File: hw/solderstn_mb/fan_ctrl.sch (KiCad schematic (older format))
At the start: 9 parts, among them M601 Fan_4pin, Q601 DMG1012T, U601 74LVC2G17gw

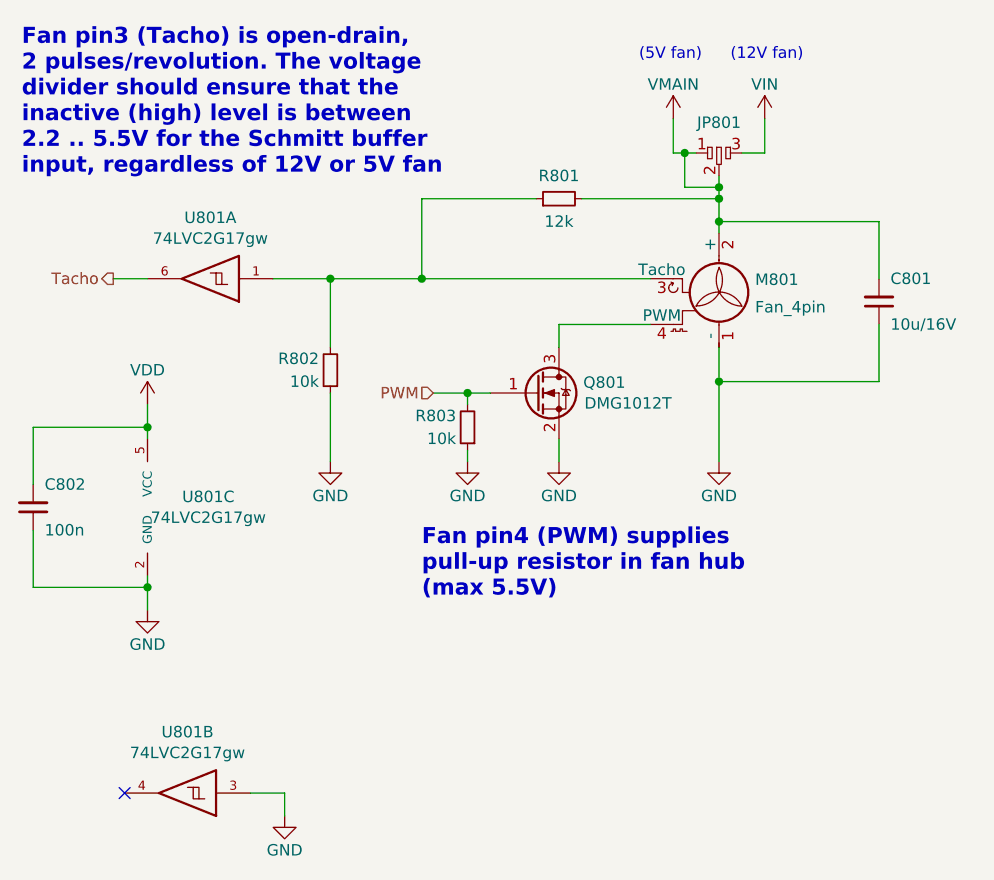
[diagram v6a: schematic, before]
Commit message: MB: 1) remove 2x fan ctrls 2) MCU pin-out for a VS1063 3) add VS1063 DSP/codec to audio path (WIP)
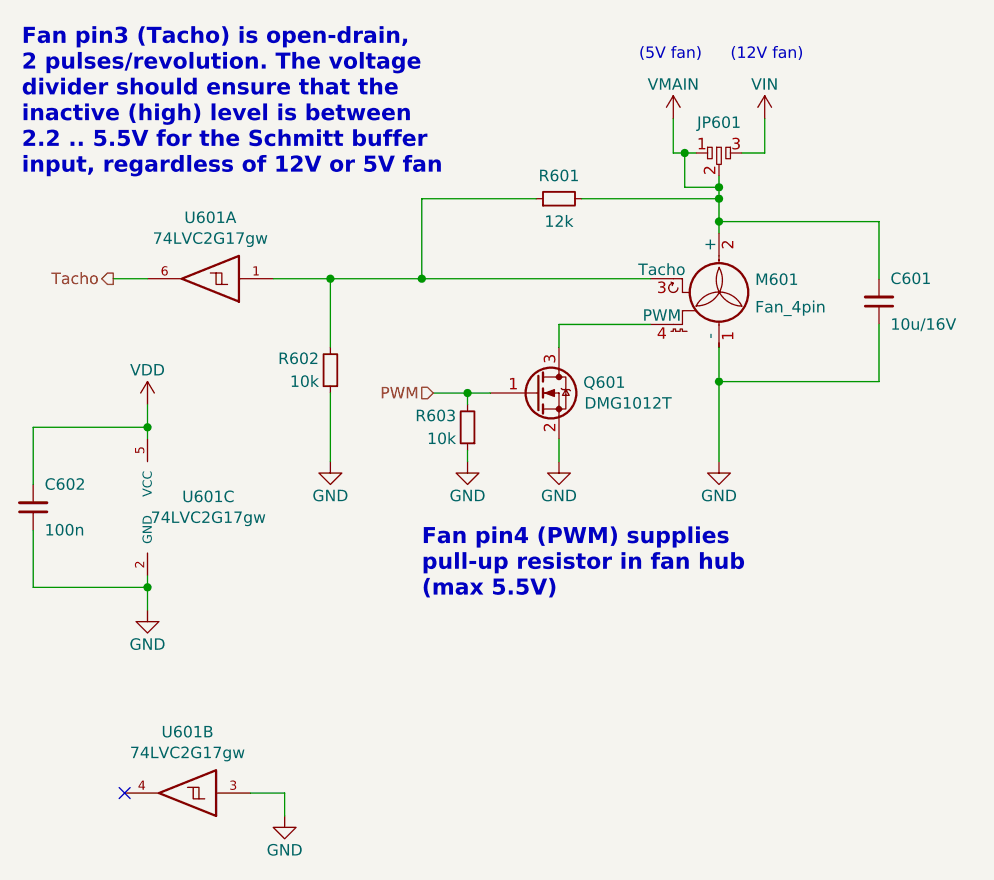
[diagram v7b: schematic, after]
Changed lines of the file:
@@
 $Descr A4 11693 8268
 encoding utf-8
-Sheet 8 23
+Sheet 8 21
 Title "Fan controller"
 Date "2020-08-09"
@@
 AR Path="/5F472FC2/5F472468/5F477A60" Ref="U701"  Part="1"
 AR Path="/5F472FC2/5F472567/5F477A60" Ref="U801"  Part="1"
-F 0 "U801" H 3225 3883 50  0000 C CNN
+F 0 "U601" H 3225 3883 50  0000 C CNN
 F 1 "74LVC2G17gw" H 3225 3974 50  0000 C CNN
 F 2 "Package_TO_SOT_SMD:SOT-363_SC-70-6_Handsoldering" H 3250 4150 50  0001 C CNN
@@
 AR Path="/5F472FC2/5F472468/5F47830A" Ref="M701"  Part="1"
 AR Path="/5F472FC2/5F472567/5F47830A" Ref="M801"  Part="1"
-F 0 "M801" H 5658 4346 50  0000 L CNN
+F 0 "M601" H 5658 4346 50  0000 L CNN
 F 1 "Fan_4pin" H 5658 4255 50  0000 L TNN
 F 2 "Connector:FanPinHeader_1x04_P2.54mm_Vertical" H 5500 4260 50  0001 C CNN
@@
 AR Path="/5F472FC2/5F472468/5F47BC77" Ref="#PWR0707"  Part="1"
 AR Path="/5F472FC2/5F472567/5F47BC77" Ref="#PWR0807"  Part="1"
-F 0 "#PWR0807" H 5500 4700 50  0001 C CNN
+F 0 "#PWR0607" H 5500 4700 50  0001 C CNN
 F 1 "GND" H 5500 4800 50  0000 C CNN
 F 2 "" H 5500 4950 50  0001 C CNN
@@
 AR Path="/5F472FC2/5F472468/5F47C1EF" Ref="#PWR0702"  Part="1"
 AR Path="/5F472FC2/5F472567/5F47C1EF" Ref="#PWR0802"  Part="1"
-F 0 "#PWR0802" H 5700 3300 50  0001 C CNN
+F 0 "#PWR0602" H 5700 3300 50  0001 C CNN
 F 1 "VIN" H 5700 3600 50  0000 C CNN
 F 2 "" H 5700 3450 50  0001 C CNN
@@
 AR Path="/5F472FC2/5F472468/5F47C86B" Ref="#PWR0701"  Part="1"
 AR Path="/5F472FC2/5F472567/5F47C86B" Ref="#PWR0801"  Part="1"
-F 0 "#PWR0801" H 5300 3300 50  0001 C CNN
+F 0 "#PWR0601" H 5300 3300 50  0001 C CNN
 F 1 "VMAIN" H 5300 3600 50  0000 C CNN
 F 2 "" H 5300 3450 50  0001 C CNN
@@
 AR Path="/5F472FC2/5F472468/5F47F331" Ref="#PWR0706"  Part="1"
 AR Path="/5F472FC2/5F472567/5F47F331" Ref="#PWR0806"  Part="1"
-F 0 "#PWR0806" H 4800 4700 50  0001 C CNN
+F 0 "#PWR0606" H 4800 4700 50  0001 C CNN
 F 1 "GND" H 4800 4800 50  0000 C CNN
 F 2 "" H 4800 4950 50  0001 C CNN
@@
 AR Path="/5F472FC2/5F472468/5F4806DE" Ref="R703"  Part="1"
 AR Path="/5F472FC2/5F472567/5F4806DE" Ref="R803"  Part="1"
-F 0 "R803" H 4450 4750 50  0000 L CNN
+F 0 "R603" H 4450 4750 50  0000 L CNN
 F 1 "10k" H 4450 4850 50  0000 L CNN
 F 2 "Resistor_SMD:R_0603_1608Metric" H 4400 4800 50  0001 C CNN
@@
 AR Path="/5F472FC2/5F472468/5F473D01" Ref="Q701"  Part="1"
 AR Path="/5F472FC2/5F472567/5F473D01" Ref="Q801"  Part="1"
-F 0 "Q801" H 4906 4696 50  0000 L CNN
+F 0 "Q601" H 4906 4696 50  0000 L CNN
 F 1 "DMG1012T" H 5102 4605 50  0000 C CNN
 F 2 "customlib_mj_fp:SOT-523" H 4900 4750 50  0001 C CNN
@@
 AR Path="/5F472FC2/5F472468/5F4818C3" Ref="#PWR0705"  Part="1"
 AR Path="/5F472FC2/5F472567/5F4818C3" Ref="#PWR0805"  Part="1"
-F 0 "#PWR0805" H 4400 4700 50  0001 C CNN
+F 0 "#PWR0605" H 4400 4700 50  0001 C CNN
 F 1 "GND" H 4400 4800 50  0000 C CNN
 F 2 "" H 4400 4950 50  0001 C CNN
@@
 AR Path="/5F472FC2/5F472468/5F483E98" Ref="R701"  Part="1"
 AR Path="/5F472FC2/5F472567/5F483E98" Ref="R801"  Part="1"
-F 0 "R801" V 4900 3800 50  0000 C CNN
+F 0 "R601" V 4900 3800 50  0000 C CNN
 F 1 "12k" V 4700 3800 50  0000 C CNN
 F 2 "Resistor_SMD:R_0603_1608Metric" H 4800 3800 50  0001 C CNN
@@
 AR Path="/5F472FC2/5F472468/5F4863E6" Ref="R702"  Part="1"
 AR Path="/5F472FC2/5F472567/5F4863E6" Ref="R802"  Part="1"
-F 0 "R802" H 3850 4500 50  0000 L CNN
+F 0 "R602" H 3850 4500 50  0000 L CNN
 F 1 "10k" H 3850 4600 50  0000 L CNN
 F 2 "Resistor_SMD:R_0603_1608Metric" H 3800 4550 50  0001 C CNN
@@
 AR Path="/5F472FC2/5F472468/5F487FE0" Ref="#PWR0704"  Part="1"
 AR Path="/5F472FC2/5F472567/5F487FE0" Ref="#PWR0804"  Part="1"
-F 0 "#PWR0804" H 3800 4700 50  0001 C CNN
+F 0 "#PWR0604" H 3800 4700 50  0001 C CNN
 F 1 "GND" H 3800 4800 50  0000 C CNN
 F 2 "" H 3800 4950 50  0001 C CNN
@@
 AR Path="/5F472FC2/5F472468/5F48A695" Ref="U701"  Part="3"
 AR Path="/5F472FC2/5F472567/5F48A695" Ref="U801"  Part="3"
-F 0 "U801" H 3266 5196 50  0000 C CNN
+F 0 "U601" H 3266 5196 50  0000 C CNN
 F 1 "74LVC2G17gw" H 3266 5105 50  0000 C CNN
 F 2 "Package_TO_SOT_SMD:SOT-363_SC-70-6_Handsoldering" H 3000 5150 50  0001 C CNN
@@
 AR Path="/5F472FC2/5F472468/5F48C2EA" Ref="#PWR0703"  Part="1"
 AR Path="/5F472FC2/5F472567/5F48C2EA" Ref="#PWR0803"  Part="1"
-F 0 "#PWR0803" H 3000 4550 50  0001 C CNN
+F 0 "#PWR0603" H 3000 4550 50  0001 C CNN
 F 1 "VDD" H 3000 4850 50  0000 C CNN
 F 2 "" H 3000 4700 50  0001 C CNN
@@
 AR Path="/5F472FC2/5F472468/5F48D304" Ref="#PWR0708"  Part="1"
 AR Path="/5F472FC2/5F472567/5F48D304" Ref="#PWR0808"  Part="1"
-F 0 "#PWR0808" H 3000 5350 50  0001 C CNN
+F 0 "#PWR0608" H 3000 5350 50  0001 C CNN
 F 1 "GND" H 3000 5450 50  0000 C CNN
 F 2 "" H 3000 5600 50  0001 C CNN
@@
 AR Path="/5F472FC2/5F472468/5F493FAA" Ref="C702"  Part="1"
 AR Path="/5F472FC2/5F472567/5F493FAA" Ref="C802"  Part="1"
-F 0 "C802" H 2550 5050 50  0000 L CNN
+F 0 "C602" H 2550 5050 50  0000 L CNN
 F 1 "100n" H 2550 5250 50  0000 L CNN
 F 2 "Capacitor_SMD:C_0603_1608Metric" H 2500 5150 50  0001 C CNN
@@
 AR Path="/5F472FC2/5F472468/5F4A2418" Ref="C701"  Part="1"
 AR Path="/5F472FC2/5F472567/5F4A2418" Ref="C801"  Part="1"
-F 0 "C801" H 6250 4150 50  0000 L CNN
+F 0 "C601" H 6250 4150 50  0000 L CNN
 F 1 "10u/16V" H 6250 4350 50  0000 L CNN
 F 2 "Capacitor_SMD:C_0603_1608Metric" H 6200 4250 50  0001 C CNN
@@
 AR Path="/5F472FC2/5F472468/5F478739" Ref="JP701"  Part="1"
 AR Path="/5F472FC2/5F472567/5F478739" Ref="JP801"  Part="1"
-F 0 "JP801" H 5500 3733 50  0000 C CNN
+F 0 "JP601" H 5500 3733 50  0000 C CNN
 F 1 "dogbone_3_ud" H 5525 3750 50  0001 C CNN
 F 2 "customlib_mj_fp:db3_ud_0402" H 5500 3600 50  0001 C CNN
@@
 AR Path="/5F472FC2/5F472468/5F7058CA" Ref="U701"  Part="2"
 AR Path="/5F472FC2/5F472567/5F7058CA" Ref="U801"  Part="2"
-F 0 "U801" H 3125 6133 50  0000 C CNN
+F 0 "U601" H 3125 6133 50  0000 C CNN
 F 1 "74LVC2G17gw" H 3125 6224 50  0000 C CNN
 F 2 "Package_TO_SOT_SMD:SOT-363_SC-70-6_Handsoldering" H 3150 6400 50  0001 C CNN
@@
 AR Path="/5F472FC2/5F472468/5F706B43" Ref="#PWR0709"  Part="1"
 AR Path="/5F472FC2/5F472567/5F706B43" Ref="#PWR0809"  Part="1"
-F 0 "#PWR0809" H 3600 6250 50  0001 C CNN
+F 0 "#PWR0609" H 3600 6250 50  0001 C CNN
 F 1 "GND" H 3600 6350 50  0000 C CNN
 F 2 "" H 3600 6500 50  0001 C CNN

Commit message: MB - Sch design: VS1063 in new audio path; Added: some new ESD, some fixups; Changes: some footprints, fixes
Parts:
- Q601: footprint customlib_mj_fp:SOT-523 -> customlib_mj_fp:SOT-523_handsoldering
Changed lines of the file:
@@
 $Descr A4 11693 8268
 encoding utf-8
-Sheet 8 21
+Sheet 6 21
 Title "Fan controller"
 Date "2020-08-09"
@@
 F 0 "Q601" H 4906 4696 50  0000 L CNN
 F 1 "DMG1012T" H 5102 4605 50  0000 C CNN
-F 2 "customlib_mj_fp:SOT-523" H 4900 4750 50  0001 C CNN
+F 2 "customlib_mj_fp:SOT-523_handsoldering" H 4900 4750 50  0001 C CNN
 F 3 "https://www.diodes.com/assets/Datasheets/ds31783.pdf" H 4700 4650 50  0001 C CNN
 	1    4700 4650
